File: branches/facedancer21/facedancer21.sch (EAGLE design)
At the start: 20 parts, among them CN1 HOST, CN2 TARGET, CN3 USB-A-S, Q1 12MHz, U1 F261X---PM64, U2 FT232RL-BASICSSOP, U4 MAX3421ESMD

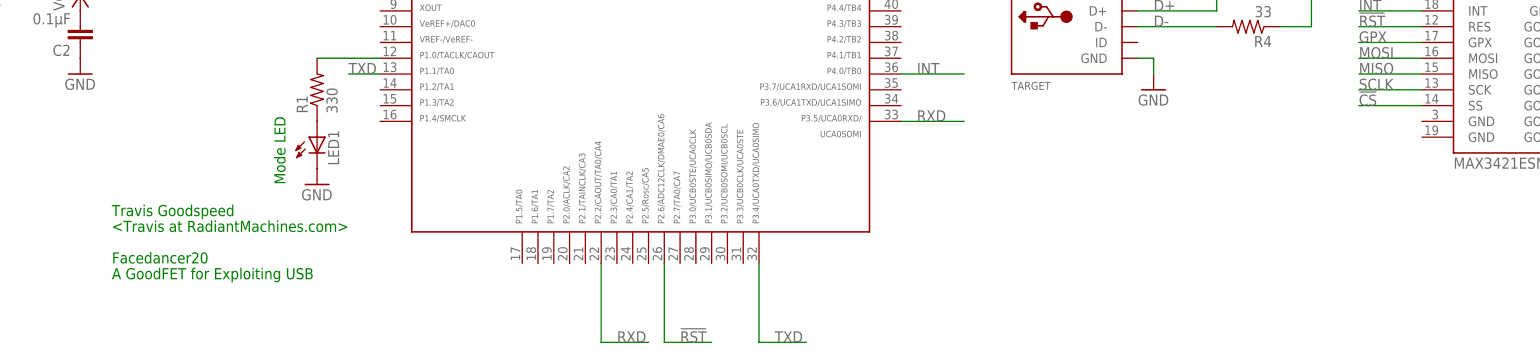
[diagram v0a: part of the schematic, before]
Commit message: FD21 fixing FD20 errata.
git-svn-id: https://svn.code.sf.net/p/goodfet/code@1378 12e2690d-a6be-4b82-a7b7-67c4a43b65c8
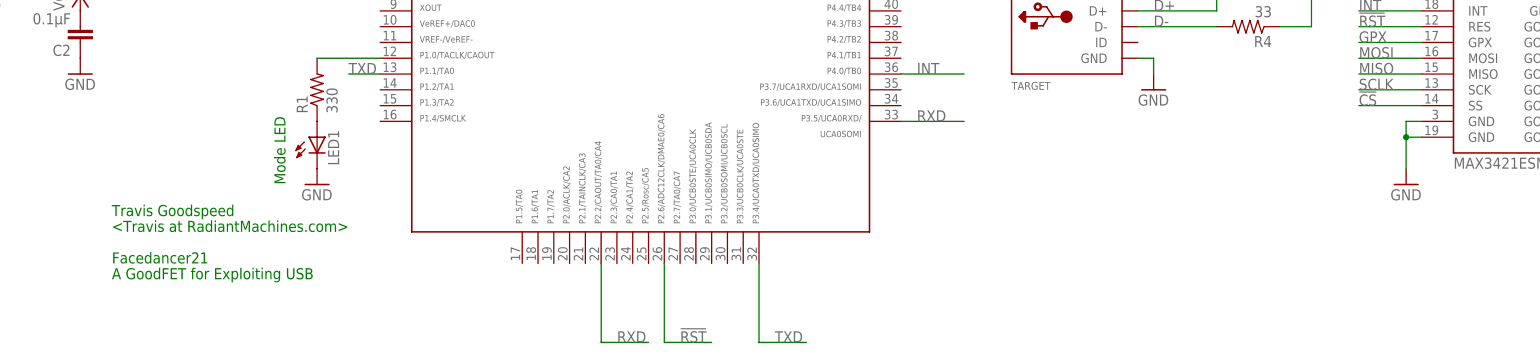
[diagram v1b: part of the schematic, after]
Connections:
- net GND: now also U4.GND@19, U4.GND@3
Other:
- note added: "Facedancer21"
- note removed: "Facedancer20"
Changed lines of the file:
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@@
 <part name="C4" library="rcl" deviceset="C-EU" device="C0603" value="0.1µF"/>
 <part name="GND7" library="supply1" deviceset="GND" device=""/>
+<part name="GND8" library="supply1" deviceset="GND" device=""/>
 </parts>
 <sheets>
@@
 <text x="0" y="15.24" size="1.778" layer="91">Travis Goodspeed</text>
 <text x="0" y="12.7" size="1.778" layer="91">&lt;Travis at RadiantMachines.com&gt;</text>
-<text x="0" y="7.62" size="1.778" layer="91">Facedancer20</text>
+<text x="0" y="7.62" size="1.778" layer="91">Facedancer21</text>
 <text x="0" y="5.08" size="1.778" layer="91">A GoodFET for Exploiting USB</text>
 </plain>
@@
 <instance part="C4" gate="G$1" x="203.2" y="73.66" rot="R270"/>
 <instance part="GND7" gate="1" x="198.12" y="63.5"/>
+<instance part="GND8" gate="1" x="208.28" y="20.32"/>
 </instances>
 <busses>
@@
 <wire x1="198.12" y1="66.04" x2="198.12" y2="73.66" width="0.1524" layer="91"/>
 </segment>
-</net>
+<segment>
+<pinref part="GND8" gate="1" pin="GND"/>
+<pinref part="U4" gate="G$1" pin="GND@3"/>
+<wire x1="208.28" y1="22.86" x2="208.28" y2="27.94" width="0.1524" layer="91"/>
+<wire x1="208.28" y1="27.94" x2="208.28" y2="30.48" width="0.1524" layer="91"/>
+<wire x1="208.28" y1="30.48" x2="210.82" y2="30.48" width="0.1524" layer="91"/>
+<pinref part="U4" gate="G$1" pin="GND@19"/>
+<wire x1="210.82" y1="27.94" x2="208.28" y2="27.94" width="0.1524" layer="91"/>
+<junction x="208.28" y="27.94"/>
+</segment>
+</net>
